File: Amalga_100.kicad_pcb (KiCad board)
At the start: 6 copper layers, 268 x 155 mm, 236 parts, among them IC1 ADM3052, IC3 INA240A1, IC4 INA240A1, IC5 INA240A1, P1 USB_B, P10 IN-, P2 Interface, P3 IN+, P4 IN-, P5 MOTOR3, P6 MOTOR2, P7 MOTOR1, P8 SWD, P9 CONN_6-HSWR-V2-rescue, Q1 IRFP4668PBF, Q10 IRFP4668PBF, Q11 IRFP4668PBF, Q12 IRFP4668PBF, Q13 BC846B, Q14 BC856B, Q15 BC846B, Q16 BC856B, Q2 IRFP4668PBF, Q3 IRFP4668PBF, Q4 IRFP4668PBF, Q5 IRFP4668PBF, Q6 IRFP4668PBF, Q7 IRFP4668PBF, Q8 IRFP4668PBF, Q9 IRFP4668PBF, SW1 SW_DIP_x02, U1 STM32F40X_LQFP64, U10 AD8664ARZ, U2 B1215S-2W, U3 JW5052C, U4 JW5052C, U5 ADUM3160, U6 AD2S1200YSTZ, U7 IRS2186, U8 IRS2186, U9 IRS2186, Y1 8MHz, Y2 8.912 MHZ

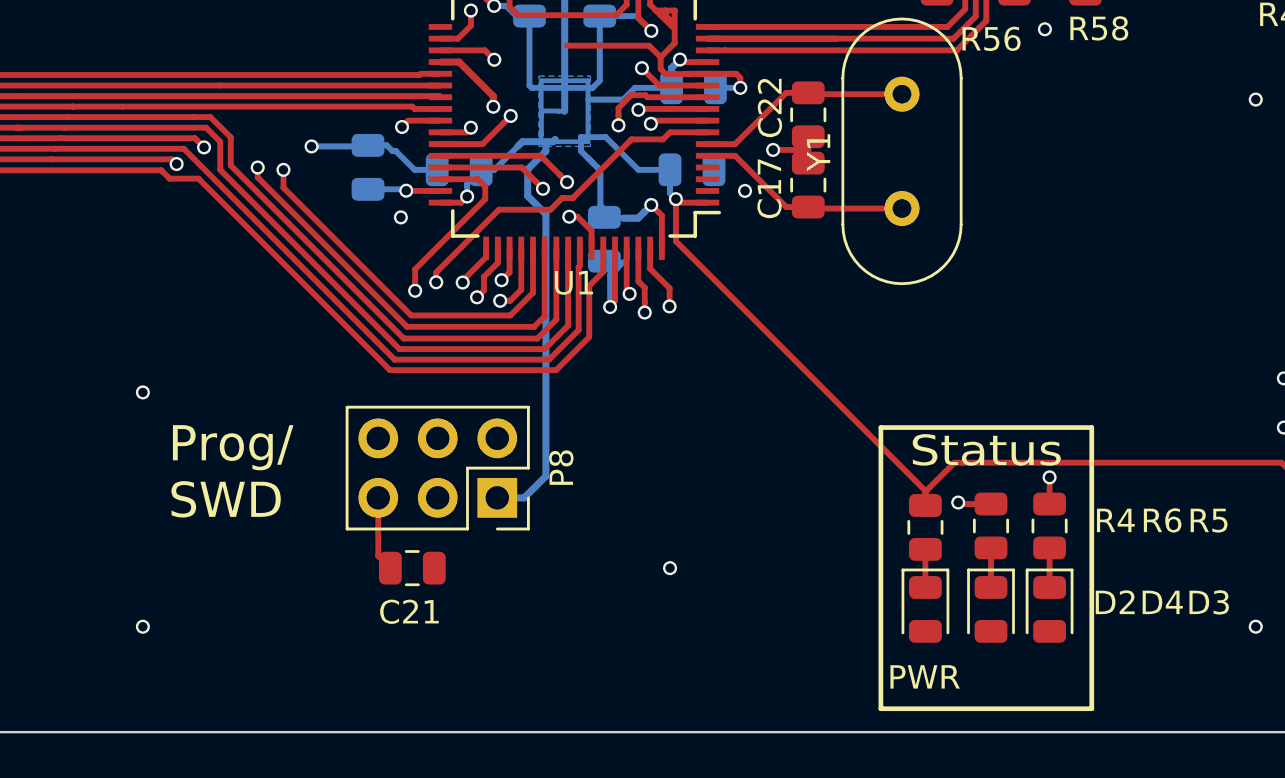
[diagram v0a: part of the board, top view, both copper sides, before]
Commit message: -changed wrong pin-header (swd)
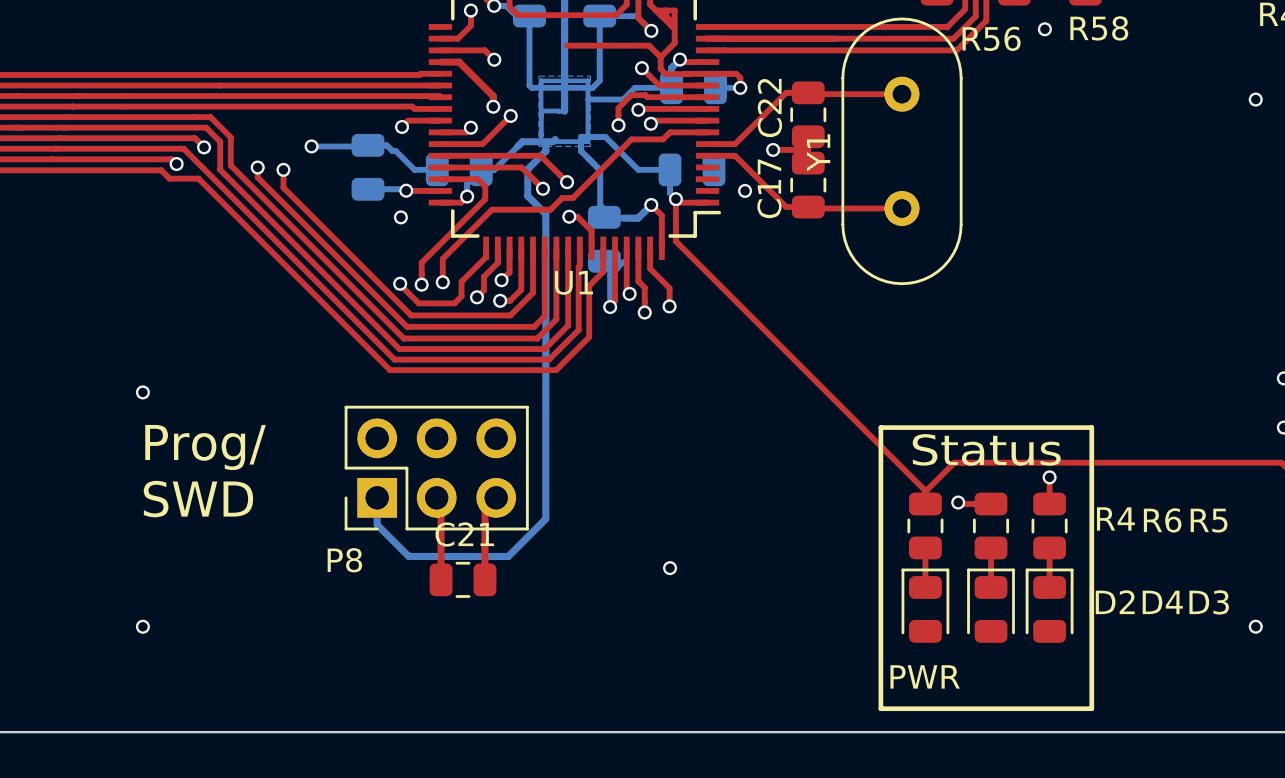
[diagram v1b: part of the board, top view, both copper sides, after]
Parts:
- C79, C80: value 10nF -> 1uF
- P8: footprint Connector_PinSocket_2.54mm:PinSocket_2x03_P2.54mm_Vertical -> Connector_PinHeader_2.54mm:PinHeader_2x03_P2.54mm_Vertical
- moved P8 5.12 mm to (158.4, 157.5), turned to 90 degrees
- moved C21 2.22 mm to (162.1, 161.0), turned to 0 degrees
- moved R4 0.06 mm to (181.8, 158.7)
- renumbered R45 to R48
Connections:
- IC1 pad 10: (no net) -> Net-(IC1-Pad10)
- P8 pad 6: (no net) -> Net-(P8-Pad6)
- U1 pad 2: (no net) -> Net-(U1-Pad2)
- U1 pad 25: (no net) -> Net-(U1-Pad25)
- U1 pad 28: (no net) -> Net-(U1-Pad28)
- U1 pad 3: (no net) -> Net-(U1-Pad3)
- U1 pad 33: (no net) -> Net-(U1-Pad33)
- U1 pad 4: (no net) -> Net-(U1-Pad4)
- U6 pad 10: (no net) -> Net-(U6-Pad10)
- U6 pad 11: (no net) -> Net-(U6-Pad11)
- U6 pad 12: (no net) -> Net-(U6-Pad12)
- U6 pad 13: (no net) -> Net-(U6-Pad13)
- U6 pad 14: (no net) -> Net-(U6-Pad14)
- U6 pad 15: (no net) -> Net-(U6-Pad15)
- U6 pad 18: (no net) -> Net-(U6-Pad18)
- U6 pad 19: (no net) -> Net-(U6-Pad19)
- U6 pad 20: (no net) -> Net-(U6-Pad20)
- U6 pad 24: (no net) -> Net-(U6-Pad24)
- U6 pad 29: (no net) -> Net-(U6-Pad29)
- U6 pad 30: (no net) -> Net-(U6-Pad30)
- U6 pad 33: (no net) -> Net-(U6-Pad33)
- U6 pad 44: (no net) -> Net-(U6-Pad44)
- U6 pad 9: (no net) -> Net-(U6-Pad9)
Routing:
- net +3V3: track 602.4 -> 611.4 mm
- net SWCLK: track 9.18 -> 13.4 mm
- net GND: track 452.1 -> 455.7 mm
- net NRST: track 30.7 -> 28.9 mm

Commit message: -changed ad2s1200 to ad2s1205  (pin compatibel) -changed excitation-buffer circuit. (AD8397 in use now) -fixed thermal-connections of planes
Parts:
- removed Q13, Q15: BC846B, Package_TO_SOT_SMD:SOT-23
- removed Q14, Q16: BC856B, Package_TO_SOT_SMD:SOT-23
- removed R11: 1Meg, Resistors_SMD:R_0805
- removed R12, R13: 15k4, Resistor_SMD:R_0805_2012Metric
- removed R69, R70, R73, R74: 2K7, Resistor_SMD:R_0805_2012Metric
- removed R71, R72, R75, R76: 33R, Resistor_SMD:R_0805_2012Metric
- added R77: 10k, Resistor_SMD:R_0805_2012Metric, F.Cu at (81.1, 149.4)
- added U11: ADM811, TO_SOT_Packages_SMD:SOT-143, F.Cu at (81.6, 153.0)
- C36: moved to F.Cu
- JP1, JP2, JP3: footprint Jumper:SolderJumper-3_P1.3mm_Bridged12_RoundedPad1.0x1.5mm -> Jumper:SolderJumper-3_P1.3mm_Open_RoundedPad1.0x1.5mm_NumberLabels
- R18: footprint Resistors_SMD:R_0805 -> Resistor_SMD:R_0805_2012Metric
- R45, R47, R48: footprint alexmod:CSS3920 -> eigene_mod:CSS3920
- U10: value AD8664ARZ -> AD8397; footprint Housings_SOIC:SOIC-14_3.9x8.7mm_Pitch1.27mm -> Package_SO:SOIC-8_3.9x4.9mm_P1.27mm
- U6: value AD2S1200YSTZ -> AD2S1205
- moved R61 33.2 mm to (108.0, 157.2), turned to 270 degrees
- moved R67 32.0 mm to (103.4, 154.1), turned to 0 degrees
- moved R68 30.8 mm to (102.4, 151.2)
- moved R64 28.8 mm to (112.0, 157.1)
- moved C37 28.4 mm to (110.0, 157.1)
- moved U10 17.6 mm to (109.6, 151.7), turned to 0 degrees
- moved C40 16.8 mm to (104.4, 151.2)
- moved C36 16.5 mm to (111.4, 147.9), turned to 180 degrees
- moved C38 7.09 mm to (114.8, 152.5), turned to 90 degrees
- moved R66 4.72 mm to (117.0, 152.5), turned to 90 degrees
- moved R65 3.16 mm to (115.9, 155.3), turned to 180 degrees
- moved SW1 1.70 mm to (77.0, 152.9)
- moved Q7 0.47 mm to (132.6, 39.5)
- moved D8 0.43 mm to (161.9, 35.9)
- moved Q2 0.41 mm to (245.4, 78.0)
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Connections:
- C37 pad 1: Net-(C37-Pad1) -> /Resolver/Buffer Circuit R2D/offset_op
- C38 pad 1: /Resolver/R1 -> Net-(C38-Pad1)
- C38 pad 2: Net-(C38-Pad2) -> /Resolver/R1
- C40 pad 1: /Resolver/R2 -> Net-(C40-Pad1)
- C40 pad 2: Net-(C40-Pad2) -> /Resolver/R2
- IC1 pad 10: Net-(IC1-Pad10) -> (no net)
- P8 pad 6: Net-(P8-Pad6) -> (no net)
- R61 pad 1: Net-(C37-Pad1) -> /Resolver/Buffer Circuit R2D/offset_op
- R64 pad 2: Net-(C37-Pad1) -> /Resolver/Buffer Circuit R2D/offset_op
- R65 pad 1: Net-(R65-Pad1) -> Net-(C38-Pad1)
- R66 pad 1: Net-(R65-Pad1) -> Net-(C38-Pad1)
- R66 pad 2: Net-(R66-Pad2) -> /Resolver/R1
- R67 pad 1: Net-(R67-Pad1) -> Net-(C40-Pad1)
- R68 pad 1: Net-(R67-Pad1) -> Net-(C40-Pad1)
- R68 pad 2: Net-(R68-Pad2) -> /Resolver/R2
- U1 pad 2: Net-(U1-Pad2) -> (no net)
- U1 pad 25: Net-(U1-Pad25) -> (no net)
- U1 pad 28: Net-(U1-Pad28) -> (no net)
- U1 pad 3: Net-(U1-Pad3) -> (no net)
- U1 pad 33: Net-(U1-Pad33) -> (no net)
- U1 pad 4: Net-(U1-Pad4) -> (no net)
- U10 pad 1: Net-(R68-Pad2) -> /Resolver/R2
- U10 pad 2: Net-(R67-Pad1) -> /Resolver/Buffer Circuit R2D/offset_op
- U10 pad 3: Net-(C37-Pad1) -> Net-(C40-Pad1)
- U10 pad 4: +15V -> GND
- U10 pad 5: Net-(R68-Pad2) -> Net-(C38-Pad1)
- U10 pad 6: Net-(C40-Pad2) -> /Resolver/Buffer Circuit R2D/offset_op
- U10 pad 7: Net-(R69-Pad2) -> /Resolver/R1
- U10 pad 8: Net-(R66-Pad2) -> +15V
- U6 pad 10: Net-(U6-Pad10) -> (no net)
- U6 pad 11: Net-(U6-Pad11) -> (no net)
- U6 pad 12: Net-(U6-Pad12) -> (no net)
- U6 pad 13: Net-(U6-Pad13) -> (no net)
- U6 pad 14: Net-(U6-Pad14) -> (no net)
- U6 pad 15: Net-(U6-Pad15) -> (no net)
- U6 pad 18: Net-(U6-Pad18) -> (no net)
- U6 pad 19: Net-(U6-Pad19) -> (no net)
- U6 pad 20: Net-(U6-Pad20) -> (no net)
- U6 pad 24: Net-(U6-Pad24) -> (no net)
- U6 pad 29: Net-(U6-Pad29) -> (no net)
- U6 pad 30: Net-(U6-Pad30) -> (no net)
- U6 pad 44: Net-(U6-Pad44) -> (no net)
- U6 pad 9: Net-(U6-Pad9) -> (no net)
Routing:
- net +15V: track 490.3 -> 453.9 mm, vias 10 -> 9
- net Net-(R73-Pad2): track 32.0 -> 0.00 mm
- net +5V: track 230.7 -> 202.6 mm, vias 6 -> 5
- net Net-(C37-Pad1): track 23.2 -> 0.00 mm
- net /Resolver/Buffer Circuit R2D/EXC: track 55.4 -> 33.6 mm
- net Net-(R69-Pad2): track 20.2 -> 0.00 mm
- net GND: track 455.7 -> 436.3 mm, vias 57 -> 56
- net Net-(C38-Pad2): track 18.1 -> 0.00 mm
- net /Resolver/Buffer Circuit R2D/offset_op: track 0.00 -> 15.8 mm
- net /Resolver/R2: track 52.1 -> 36.4 mm
- net H2_VS: track 143.6 -> 158.7 mm, vias 47 -> 48
- net H3_VS: track 224.2 -> 238.4 mm, vias 46 -> 47
- net Net-(R68-Pad2): track 10.1 -> 0.00 mm
- net Net-(R66-Pad2): track 10.00 -> 0.00 mm
- net /USB-Isolator/GND1: track 58.9 -> 50.0 mm
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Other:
- board text added: "prim. to sec. (R66/R68) 1:2 25k 1:1 50k 2:1 100k 5:1 250k"
- board text removed: "prim. to sec. Ohm 1:2 25k 1:1 50k 2:1 100k 5:1 250k"

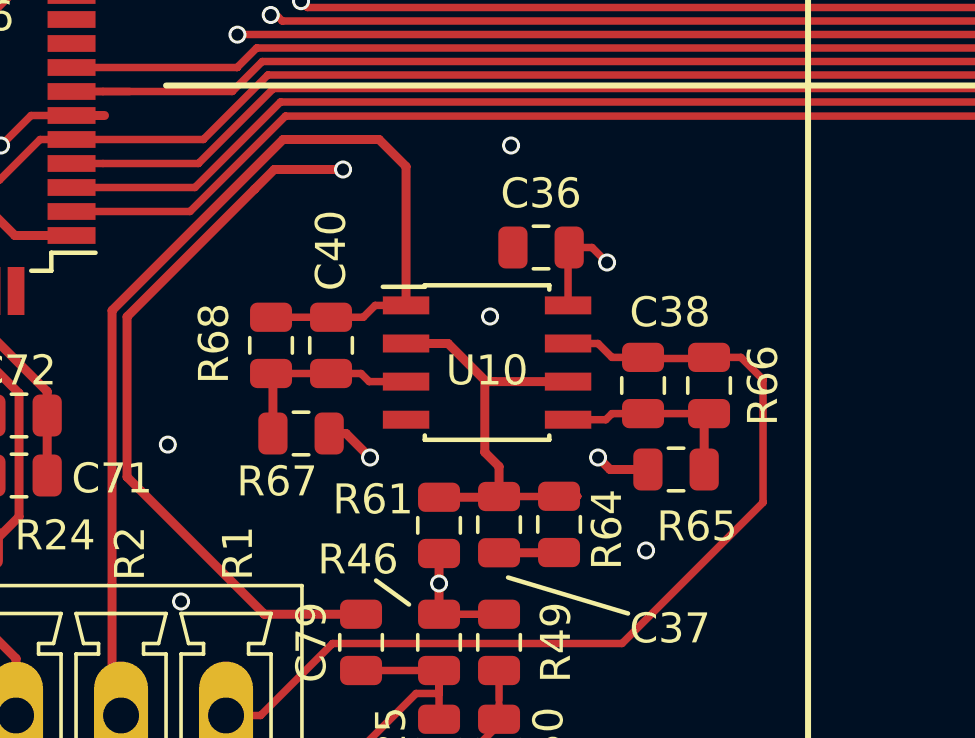
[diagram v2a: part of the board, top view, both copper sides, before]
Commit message: -fixed wrong connection on +/- of opamp in exc-buffer
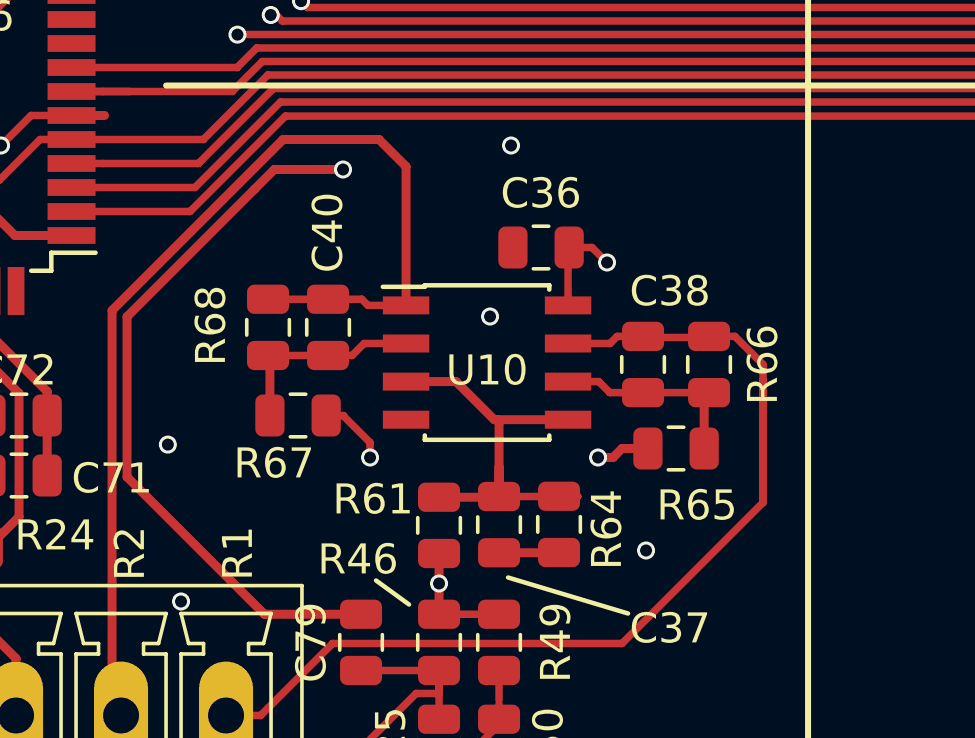
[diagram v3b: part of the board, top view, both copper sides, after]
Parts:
- moved R65 0.70 mm to (115.9, 154.6)
- moved C38 0.70 mm to (114.8, 151.8)
- moved R66 0.70 mm to (117.0, 151.8)
- moved C40 0.61 mm to (104.3, 150.6)
- moved R67 0.61 mm to (103.3, 153.5)
- moved R68 0.61 mm to (102.3, 150.6)
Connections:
- U10 pad 2: /Resolver/Buffer Circuit R2D/offset_op -> Net-(C40-Pad1)
- U10 pad 3: Net-(C40-Pad1) -> /Resolver/Buffer Circuit R2D/offset_op
- U10 pad 5: Net-(C38-Pad1) -> /Resolver/Buffer Circuit R2D/offset_op
- U10 pad 6: /Resolver/Buffer Circuit R2D/offset_op -> Net-(C38-Pad1)
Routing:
- net /Resolver/R1: track 32.6 -> 37.2 mm
- net /Resolver/Buffer Circuit R2D/offset_op: track 15.8 -> 14.9 mm
- net /Resolver/Buffer Circuit R2D/EXC: track 33.6 -> 34.2 mm
- net Net-(C38-Pad1): track 6.71 -> 7.26 mm

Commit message: -finished and Tagged Layout -createt Gerber-Files
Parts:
- moved D12 0.10 mm to (135.4, 35.6)
- moved Q7 0.10 mm to (132.7, 39.5)
- moved Y2 0.10 mm to (88.9, 128.6)
- moved C46 0.08 mm to (104.3, 120.2)
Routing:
- net GND: track 436.3 -> 419.7 mm
- net +BATT: track 74.8 -> 89.4 mm
- net H3_VS: track 238.4 -> 246.2 mm, vias 47 -> 46
- net H1_VS: track 161.0 -> 166.4 mm, vias 49 -> 48
- net +15V: track 453.9 -> 458.4 mm
- net H2_VS: track 158.7 -> 161.8 mm, vias 48 -> 47
- net /MCU/SCK_ADC_EXT: track 163.8 -> 162.8 mm
- net /MCU/MISO_ADC_EXT2: track 154.5 -> 153.6 mm
- net /MCU/SERVO: track 173.7 -> 174.6 mm
- net /MCU/RX_SDA_NSS: track 174.0 -> 174.9 mm
- net /MCU/BR_SO1: track 149.9 -> 149.1 mm
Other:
- board text added: "Gain (R66/R68) 0.5 50k 1.0 100k 2.0 200k 5.0 500k"
- board text removed: "prim. to sec. (R66/R68) 1:2 25k 1:1 50k 2:1 100k 5:1 250k"

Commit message: BU
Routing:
- net H1_VS: track 166.4 -> 169.8 mm
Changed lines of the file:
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@@
     (thickness 1.6)
     (drawings 85)
-    (tracks 4039)
+    (tracks 4043)
     (zones 0)
     (modules 223)
@@
   (page A4)
   (layers
-    (0 "F.Cu_(top)" signal hide)
+    (0 "F.Cu_(top)" signal)
     (1 inner_layer1 power hide)
     (2 inner_layer2 power hide)
@@
   )
   (setup
-    (last_trace_width 0.3)
+    (last_trace_width 0.6)
     (user_trace_width 0.2)
     (user_trace_width 0.25)
@@
   (segment (start 245.71 73.41) (end 244.9 72.6) (width 1) (layer "B.Cu_(GND_bottom)") (net 98))
   (segment (start 244.9 71.6) (end 245.4 71.1) (width 1) (layer "B.Cu_(GND_bottom)") (net 98))
-  (segment (start 244.9 72.6) (end 244.9 71.6) (width 1) (layer "B.Cu_(GND_bottom)") (net 98))
+  (segment (start 244.77 72.58) (end 244.77 71.58) (width 0.8) (layer "B.Cu_(GND_bottom)") (net 98))
   (segment (start 246.1 68.4) (end 246.1 66.7) (width 1) (layer "B.Cu_(GND_bottom)") (net 98))
   (segment (start 245.4 71.1) (end 245.4 69.1) (width 1) (layer "B.Cu_(GND_bottom)") (net 98))
@@
   (segment (start 240.9 42.3) (end 240.8 42.2) (width 0.6) (layer "F.Cu_(top)") (net 98))
   (segment (start 240.8 42.2) (end 240.8 41.3) (width 0.6) (layer "F.Cu_(top)") (net 98))
+  (segment (start 245.4 74) (end 245.4 73.23) (width 0.6) (layer "B.Cu_(GND_bottom)") (net 98))
+  (segment (start 245.4 73.23) (end 246.09 72.54) (width 0.6) (layer "B.Cu_(GND_bottom)") (net 98))
+  (segment (start 246.09 71.79) (end 245.4 71.1) (width 0.6) (layer "B.Cu_(GND_bottom)") (net 98))
+  (segment (start 246.02 72.45) (end 246.02 71.7) (width 0.8) (layer "B.Cu_(GND_bottom)") (net 98))
   (via (at 49.9 75) (size 0.6) (drill 0.4) (layers "F.Cu_(top)" "B.Cu_(GND_bottom)") (net 99))
   (segment (start 44.187351 76.312649) (end 44.574999 75.925001) (width 0.45) (layer "B.Cu_(GND_bottom)") (net 99))
